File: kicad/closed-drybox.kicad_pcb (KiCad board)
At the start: 2 copper layers, 99.5 x 99.6 mm, 35 parts, among them J1 Power_Jack, M1 Fan, M2 Fan, Q1 AO3400A, Q2 AO3400A, Q3 AO3400A, Q4 AO3400A, Q5 AO3400A, Q6 AO3400A, Q7 AO3400A, U1 AMS1117-3.3, U2 XIAO-ESP32-C6, U3 INA219AxDCN

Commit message: pcb design v0.2
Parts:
- removed JP1: SolderJumper_2_Open, Jumper:SolderJumper-2_P1.3mm_Open_RoundedPad1.0x1.5mm
- added J10: Conn_01x02_Pin, Connector_PinHeader_2.54mm:PinHeader_1x02_P2.54mm_Vertical, F.Cu at (226.8, 65.5)
- added J2: Power_Jack, Connector_BarrelJack:BarrelJack_Horizontal, F.Cu at (215.2, 111.5)
- added J3: Conn_01x02_Pin, Connector_PinHeader_2.54mm:PinHeader_1x02_P2.54mm_Vertical, F.Cu at (209.5, 106.5)
- added J4: Conn_01x02_Pin, Connector_PinHeader_2.54mm:PinHeader_1x02_P2.54mm_Vertical, F.Cu at (218.5, 92.8)
- added J5: Conn_01x02_Pin, Connector_PinHeader_2.54mm:PinHeader_1x02_P2.54mm_Vertical, F.Cu at (203.2, 92.0)
- added J6: Conn_01x05_Pin, Connector_PinHeader_2.54mm:PinHeader_1x05_P2.54mm_Vertical, F.Cu at (203.2, 85.6)
- added J7: Conn_01x04, Connector_JST:JST_XH_B4B-XH-AM_1x04_P2.50mm_Vertical, F.Cu at (219.5, 57.0)
- added J8: Conn_01x04, Connector_JST:JST_XH_B4B-XH-AM_1x04_P2.50mm_Vertical, F.Cu at (212.0, 57.0)
- added J9: Conn_01x04, Connector_JST:JST_XH_B4B-XH-AM_1x04_P2.50mm_Vertical, F.Cu at (204.5, 57.1)
- added R10: Heater, Connector_JST:JST_XH_S2B-XH-A_1x02_P2.50mm_Horizontal, F.Cu at (169.4, 66.5)
- added R11: 4.7k, Resistor_SMD:R_0603_1608Metric_Pad0.98x0.95mm_HandSolder, F.Cu at (181.9, 69.1)
- added R12: Heater, Connector_JST:JST_XH_S2B-XH-A_1x02_P2.50mm_Horizontal, F.Cu at (169.4, 57.0)
- added R13: 4.7k, Resistor_SMD:R_0603_1608Metric_Pad0.98x0.95mm_HandSolder, F.Cu at (181.8, 59.5)
- added R9: 4.7k, Resistor_SMD:R_0603_1608Metric_Pad0.98x0.95mm_HandSolder, F.Cu at (182.2, 78.6)
- added TP1: TestPoint, TestPoint:TestPoint_Pad_D2.5mm, F.Cu at (214.0, 102.5)
- added TP10: TestPoint, TestPoint:TestPoint_Pad_D2.5mm, F.Cu at (199.0, 80.5)
- added TP11: TestPoint, TestPoint:TestPoint_Pad_D2.5mm, F.Cu at (195.5, 78.0)
- added TP12: TestPoint, TestPoint:TestPoint_Pad_D2.5mm, F.Cu at (199.0, 75.5)
- added TP13: TestPoint, TestPoint:TestPoint_Pad_D2.5mm, F.Cu at (199.0, 92.0)
- added TP14: TestPoint, TestPoint:TestPoint_Pad_D2.5mm, F.Cu at (195.5, 89.5)
- added TP15: TestPoint, TestPoint:TestPoint_Pad_D2.5mm, F.Cu at (174.5, 115.4)
- added TP16: TestPoint, TestPoint:TestPoint_Pad_D2.5mm, F.Cu at (174.4, 106.5)
- added TP26: TestPoint, TestPoint:TestPoint_Pad_D2.5mm, F.Cu at (226.8, 61.0)
- added TP27: TestPoint, TestPoint:TestPoint_Pad_D2.5mm, F.Cu at (224.2, 58.0)
- added TP3: TestPoint, TestPoint:TestPoint_Pad_D2.5mm, F.Cu at (174.5, 97.5)
- added TP4: TestPoint, TestPoint:TestPoint_Pad_D2.5mm, F.Cu at (174.5, 88.0)
- added TP5: TestPoint, TestPoint:TestPoint_Pad_D2.5mm, F.Cu at (174.5, 78.5)
- added TP6: TestPoint, TestPoint:TestPoint_Pad_D2.5mm, F.Cu at (174.5, 69.0)
- added TP7: TestPoint, TestPoint:TestPoint_Pad_D2.5mm, F.Cu at (174.5, 59.5)
- added TP8: TestPoint, TestPoint:TestPoint_Pad_D2.5mm, F.Cu at (199.0, 85.5)
- added TP9: TestPoint, TestPoint:TestPoint_Pad_D2.5mm, F.Cu at (195.5, 83.0)
- C1, C6: footprint Capacitor_SMD:C_1206_3216Metric -> Capacitor_SMD:C_0603_1608Metric
- J1: value Power_Jack -> Conn_01x02; footprint Connector_BarrelJack:BarrelJack_Horizontal -> Connector_JST:JST_XH_S2B-XH-A-1_1x02_P2.50mm_Horizontal
- R1, R2: value Heater -> 10k; footprint Connector_JST:JST_XH_S2B-XH-A_1x02_P2.50mm_Horizontal -> Resistor_SMD:R_0603_1608Metric
- R3: value Heater -> 0.1; footprint Connector_JST:JST_XH_S2B-XH-A_1x02_P2.50mm_Horizontal -> Resistor_SMD:R_2512_6332Metric
- R5: value Heater -> 4.7k; footprint Connector_JST:JST_XH_S2B-XH-A_1x02_P2.50mm_Horizontal -> Resistor_SMD:R_0603_1608Metric_Pad0.98x0.95mm_HandSolder
- R6: value 10k -> Heater; footprint Resistor_SMD:R_0603_1608Metric -> Connector_JST:JST_XH_S2B-XH-A_1x02_P2.50mm_Horizontal
- R7: value 10k -> 4.7k; footprint Resistor_SMD:R_0603_1608Metric -> Resistor_SMD:R_0603_1608Metric_Pad0.98x0.95mm_HandSolder
- R8: value 0.1 -> Heater; footprint Resistor_SMD:R_2512_6332Metric -> Connector_JST:JST_XH_S2B-XH-A_1x02_P2.50mm_Horizontal
- U1: value AMS1117-3.3 -> AMS1117-5.0
- moved H2 152.5 mm to (164.0, 50.5)
- moved R8 82.0 mm to (169.5, 76.0), turned to -90 degrees
- moved R6 78.1 mm to (169.4, 85.5)
- moved H4 73.9 mm to (225.0, 121.5)
- moved H1 71.8 mm to (225.0, 50.5)
- moved R7 67.8 mm to (182.0, 88.0), turned to 90 degrees
- moved Q1 52.4 mm to (179.0, 97.4)
- moved C7 51.9 mm to (200.9, 117.5), turned to 90 degrees
- moved Q2 51.8 mm to (179.1, 88.0)
- moved C2 50.9 mm to (199.3, 100.9), turned to 90 degrees
- moved C1 50.8 mm to (197.8, 101.0), turned to 90 degrees
- moved C3 50.4 mm to (201.1, 100.9)
- moved H3 46.8 mm to (163.8, 121.5)
- moved Q5 45.0 mm to (178.9, 59.5)
- moved R1 43.5 mm to (202.7, 117.5)
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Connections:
- C4 pad 1: +3.3V -> Net-(J4-Pin_1)
- C5 pad 1: +3.3V -> Net-(J4-Pin_1)
- C6 pad 1: +3.3V -> Net-(J4-Pin_1)
- J1 pad 1: /power measurement/IN -> GND
- J1 pad 2: GND -> /power measurement/IN
- M1 pad 2: Net-(D2-A) -> Net-(D1-A)
- M2 pad 2: Net-(D1-A) -> Net-(D2-A)
- Q1 pad 1: /FAN1 -> /HEAT1
- Q1 pad 3: Net-(D1-A) -> Net-(Q1-D)
- Q2 pad 1: /FAN2 -> /HEAT2
- Q2 pad 3: Net-(D2-A) -> Net-(Q2-D)
- Q3 pad 1: /HEAT1 -> /HEAT3
- Q4 pad 1: /HEAT2 -> /HEAT4
- Q5 pad 1: /HEAT3 -> /HEAT5
- Q6 pad 1: /HEAT4 -> /FAN1
- Q6 pad 3: Net-(Q6-D) -> Net-(D1-A)
- Q7 pad 1: /HEAT5 -> /FAN2
- Q7 pad 3: Net-(Q7-D) -> Net-(D2-A)
- R1 pad 1: +12V -> +3.3V
- R1 pad 2: Net-(Q3-D) -> /SDA
- R2 pad 1: +12V -> +3.3V
- R2 pad 2: Net-(Q4-D) -> /SCL
- R3 pad 1: +12V -> /power measurement/IN
- R3 pad 2: Net-(Q5-D) -> +12V
- R4 pad 2: Net-(Q6-D) -> Net-(Q1-D)
- R5 pad 1: +12V -> /HEAT1
- R5 pad 2: Net-(Q7-D) -> GND
- R6 pad 1: +3.3V -> +12V
- R6 pad 2: /SDA -> Net-(Q2-D)
- R7 pad 1: +3.3V -> /HEAT2
- R7 pad 2: /SCL -> GND
- R8 pad 1: /power measurement/IN -> +12V
- R8 pad 2: +12V -> Net-(Q3-D)
- U1 pad 2: +3.3V -> Net-(J4-Pin_1)
- U2 pad 1: unconnected-(U2-GPIO0/A0/D0-Pad1)_1 -> /GPIO0
- U2 pad 14: unconnected-(U2-VBUS-Pad14)_1 -> +5V
- U2 pad 2: unconnected-(U2-GPIO1/A1/D1-Pad2) -> /GPIO1
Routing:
- net +12V: track 383.7 -> 63.9 mm, vias 13 -> 51
- net /SDA: track 47.9 -> 109.5 mm, vias 2 -> 3
- net /SCL: track 53.4 -> 101.9 mm, vias 2 -> 3
- net /FAN2: track 91.0 -> 45.2 mm, vias 2 -> 4
- net +3.3V: track 61.8 -> 100.4 mm
- net /FAN1: track 85.9 -> 51.8 mm, vias 2 -> 4
- net Net-(J4-Pin_1): track 0.00 -> 18.8 mm
- net /GPIO1: track 0.00 -> 14.5 mm
- net /HEAT3: track 31.3 -> 44.3 mm, vias 1 -> 4
- net /GPIO0: track 0.00 -> 11.5 mm
- net Net-(Q2-D): track 0.00 -> 8.70 mm
- net Net-(Q6-D): track 8.69 -> 0.00 mm
- net /HEAT2: track 44.0 -> 35.4 mm, vias 1 -> 4
- net Net-(Q1-D): track 0.00 -> 8.60 mm
- net Net-(Q7-D): track 8.60 -> 0.00 mm
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- added copper zone on In2.Cu, net +12V
- added copper zone on In1.Cu, net GND
- added copper zone on In2.Cu, net GND
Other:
- board size 99.5 x 99.6 mm -> 70 x 80 mm
- copper layers 2 -> 4
- board text added: "${TITLE} (rev. ${REVISION}) by ${COMPANY} ${COMMENT1}"
- board text removed: "${TITLE} by ${COMPANY} (rev. ${REVISION}) ${COMMENT1}"

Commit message: review with @lukstruck
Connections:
- J2 pad 3: (no net) -> GND
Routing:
- net GND: track 31.1 -> 10.7 mm, vias 39 -> 9
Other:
- board text added: "C7 should be closest to IC"
- board text added: "Cap placement and power paths"
- board text added: "DS18B20?"
- board text added: "Triple check antenna cutout"
- board text added: "add pulldown to fan"
- board text added: "add temp probe? AHT20 -> pinout!"
- board text added: "change order of VIA / Diode + Testpad"
- board text added: "{ "ViaStitching": "0.2", "GND": { "HSpacing": "0.5", "VSpacing": "0.5", "HOffset": "0", "VOffset": "0", "Clearance": "0.2", "Randomize": false } }"
- board text added: "{ "ViaStitching": "0.2", "GND": { "HSpacing": "1", "VSpacing": "1", "HOffset": "0", "VOffset": "0", "Clearance": "0", "Randomize": false } }"
- board text added: "{ "ViaStitching": "0.2", "GND": { "HSpacing": "1", "VSpacing": "1", "HOffset": "0", "VOffset": "0", "Clearance": "0.3", "Randomize": false } }"

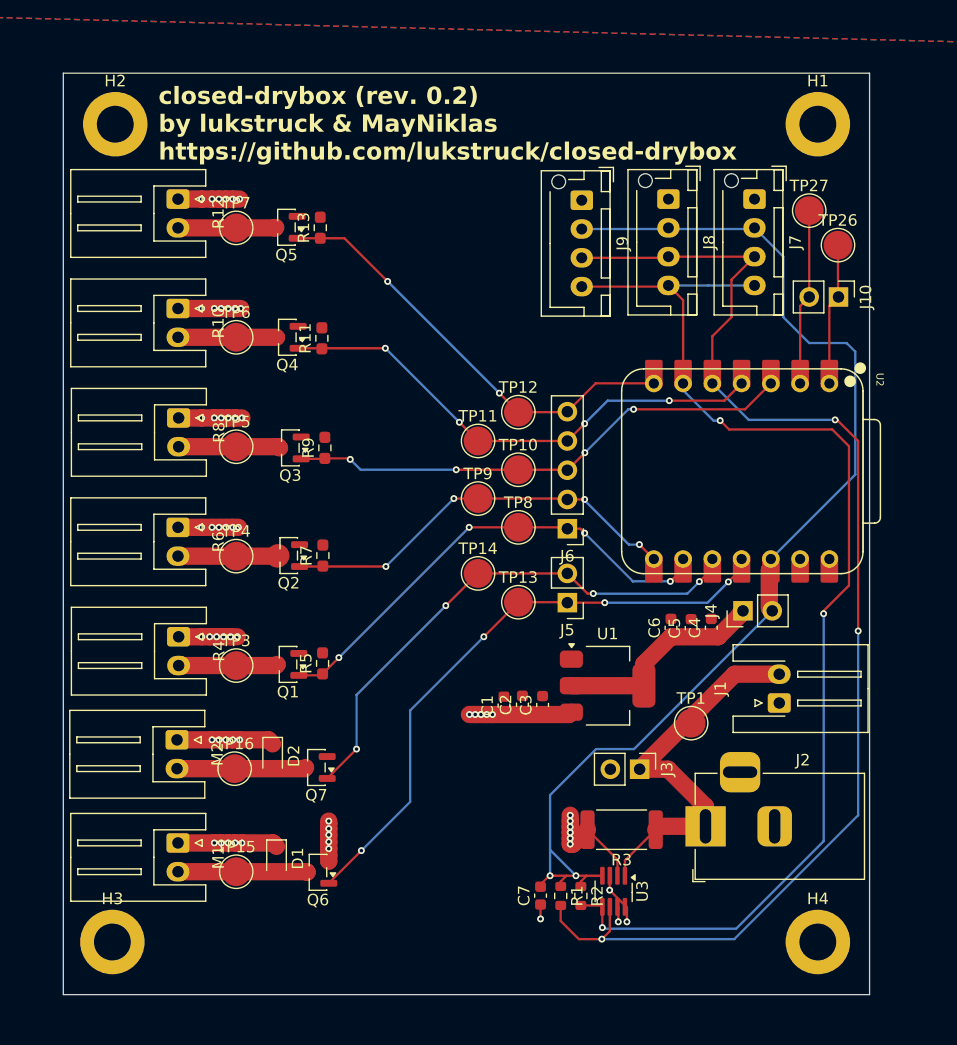
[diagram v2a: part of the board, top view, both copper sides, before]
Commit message: change routing, fix capactitors, add pulldown resistors
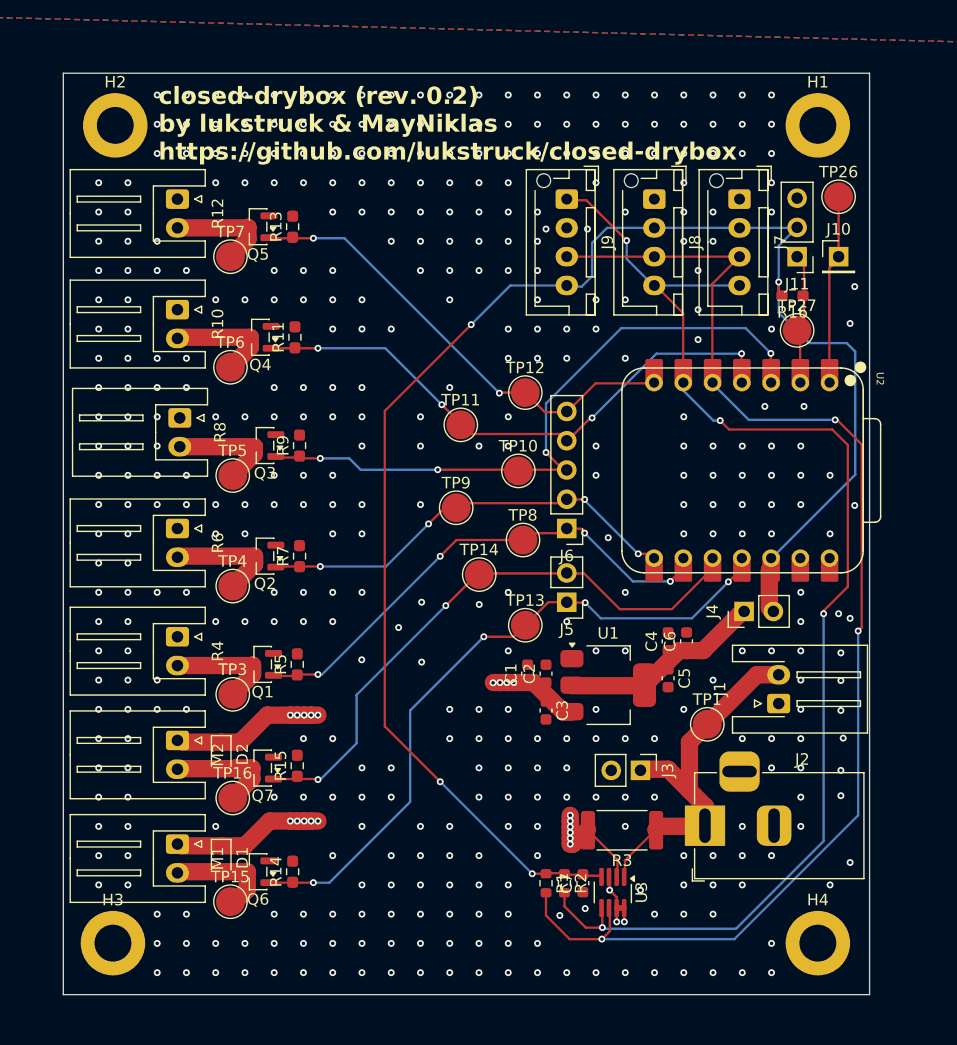
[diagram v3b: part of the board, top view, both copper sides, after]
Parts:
- added J11: Conn_01x03_Pin, Connector_PinHeader_2.54mm:PinHeader_1x03_P2.54mm_Vertical, F.Cu at (223.2, 62.0)
- added R14: 4.7k, Resistor_SMD:R_0603_1608Metric_Pad0.98x0.95mm_HandSolder, F.Cu at (179.4, 115.4)
- added R15: 4.7k, Resistor_SMD:R_0603_1608Metric_Pad0.98x0.95mm_HandSolder, F.Cu at (179.8, 106.2)
- added R16: 4.7k, Resistor_SMD:R_0603_1608Metric_Pad0.98x0.95mm_HandSolder, F.Cu at (222.8, 65.4)
- J10: value Conn_01x02_Pin -> Conn_01x01_Pin; footprint Connector_PinHeader_2.54mm:PinHeader_1x02_P2.54mm_Vertical -> Connector_PinHeader_2.54mm:PinHeader_1x01_P2.54mm_Vertical
- moved TP27 10.5 mm to (223.2, 68.4)
- moved Q6 5.20 mm to (176.4, 115.4)
- moved D1 4.80 mm to (173.2, 114.2)
- moved C5 4.79 mm to (212.0, 98.6), turned to -90 degrees
- moved Q7 4.66 mm to (176.8, 106.4)
- moved D2 4.47 mm to (173.2, 105.2)
- moved TP26 4.20 mm to (226.8, 56.8)
- moved C4 3.93 mm to (212.0, 95.4)
- moved C7 3.83 mm to (204.6, 116.4)
- moved J10 3.50 mm to (226.8, 62.0), turned to 0 degrees
- moved C1 3.45 mm to (199.8, 98.2)
- moved C2 3.39 mm to (201.4, 98.2)
- moved TP15 2.65 mm to (174.0, 118.0)
- moved TP6 2.65 mm to (174.0, 71.6)
- moved TP4 2.62 mm to (174.2, 90.6)
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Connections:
- J9 pad 1: GND -> /SCL
- J9 pad 2: +3.3V -> GND
- J9 pad 4: /SCL -> +3.3V
- TP27 pad 1: /GPIO1 -> /TEMP
- U2 pad 2: /GPIO1 -> /TEMP
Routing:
- net +3.3V: track 100.4 -> 138.1 mm, vias 2 -> 4
- net +12V: track 63.9 -> 43.2 mm, vias 51 -> 20
- net /GPIO1: track 14.5 -> 0.00 mm
- net /HEAT3: track 44.3 -> 57.5 mm
- net /TEMP: track 0.00 -> 10.8 mm
- net /SCL: track 102.0 -> 109.3 mm, vias 3 -> 4
- net /FAN1: track 51.8 -> 58.1 mm
- net /FAN2: track 45.2 -> 50.7 mm, vias 4 -> 2
- net /HEAT4: track 43.9 -> 49.1 mm
- net GND: track 10.7 -> 6.29 mm, vias 9 -> 426
- net /GPIO0: track 11.5 -> 15.7 mm
- net /HEAT5: track 38.3 -> 40.7 mm
- net /HEAT1: track 41.1 -> 43.1 mm
- net /HEAT2: track 35.4 -> 37.4 mm
- net Net-(D1-A): track 11.2 -> 9.46 mm
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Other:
- board text removed: "C7 should be closest to IC"
- board text removed: "Cap placement and power paths"
- board text removed: "DS18B20?"
- board text removed: "Triple check antenna cutout"
- board text removed: "add pulldown to fan"
- board text removed: "add temp probe? AHT20 -> pinout!"
- board text removed: "change order of VIA / Diode + Testpad"

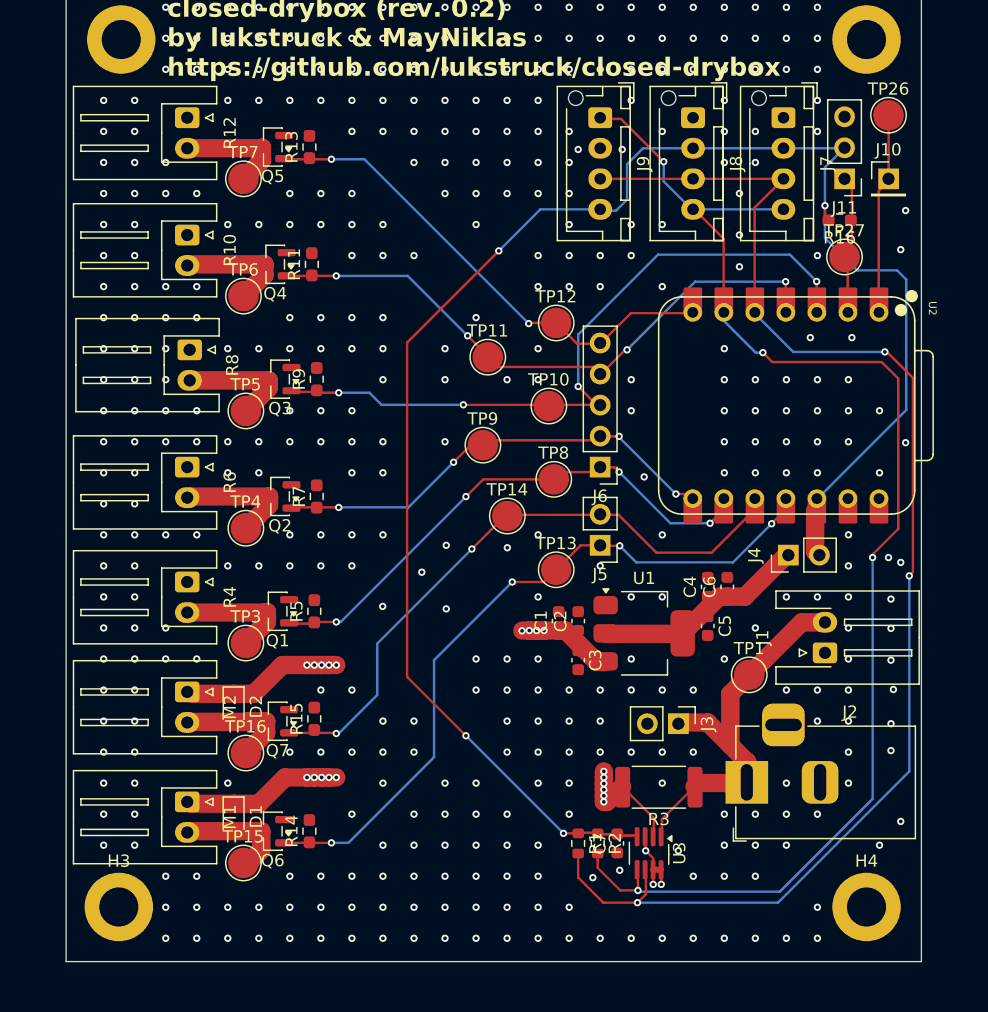
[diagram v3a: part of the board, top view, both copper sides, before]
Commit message: improve label placing, change footprints of connectors
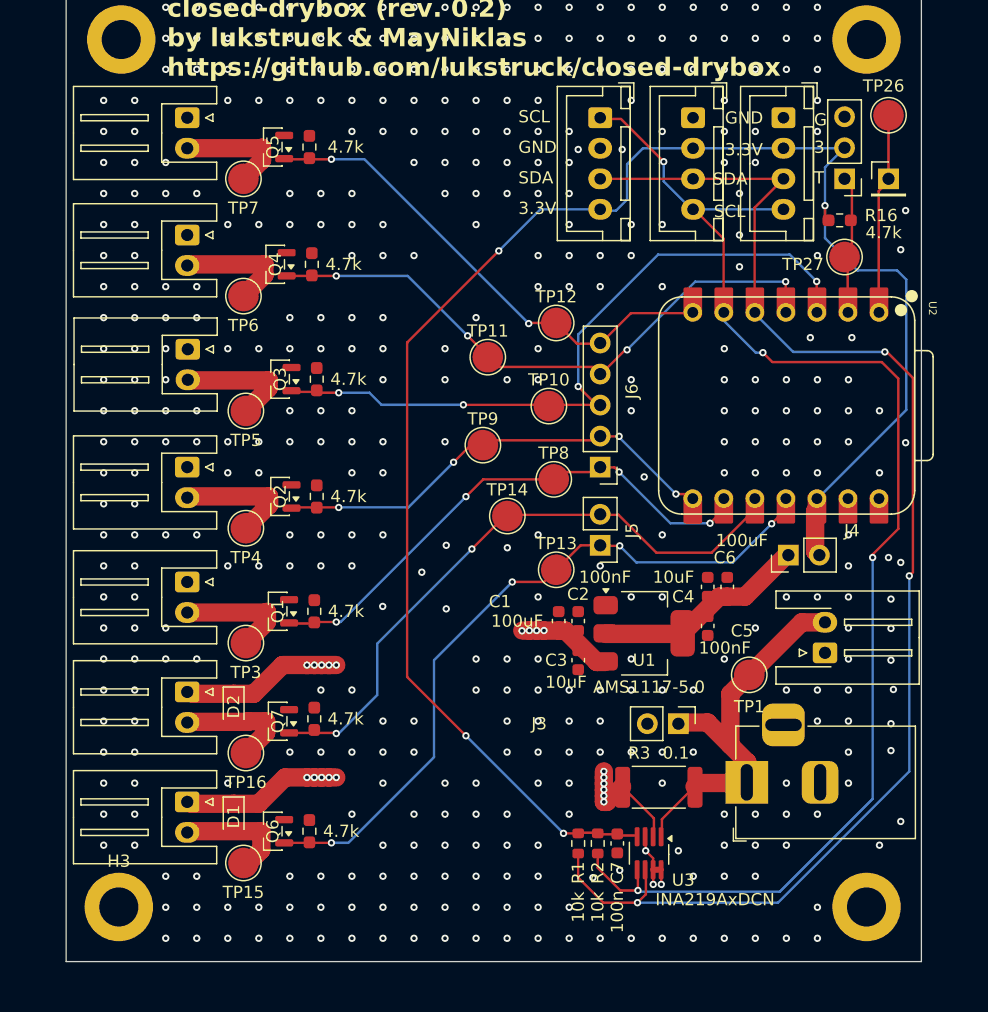
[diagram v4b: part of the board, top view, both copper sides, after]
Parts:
- J7, J8, J9: footprint Connector_JST:JST_XH_B4B-XH-AM_1x04_P2.50mm_Vertical -> Connector_JST:JST_XH_B4B-XH-A_1x04_P2.50mm_Vertical
- moved R8 0.16 mm to (169.4, 76.0)
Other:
- board text added: "3"
- board text added: "3.3V"
- board text added: "G"
- board text added: "GND"
- board text added: "SCL"
- board text added: "SDA"
- board text added: "T"
